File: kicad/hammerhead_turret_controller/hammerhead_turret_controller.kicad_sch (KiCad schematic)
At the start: 7 parts, among them J1 PLATFORM_CONN, J2 B4B-XH-A, J3 B4B-XH-A, J4 B6B-XH-A_LF__SN_, J5 B6B-XH-A_LF__SN_

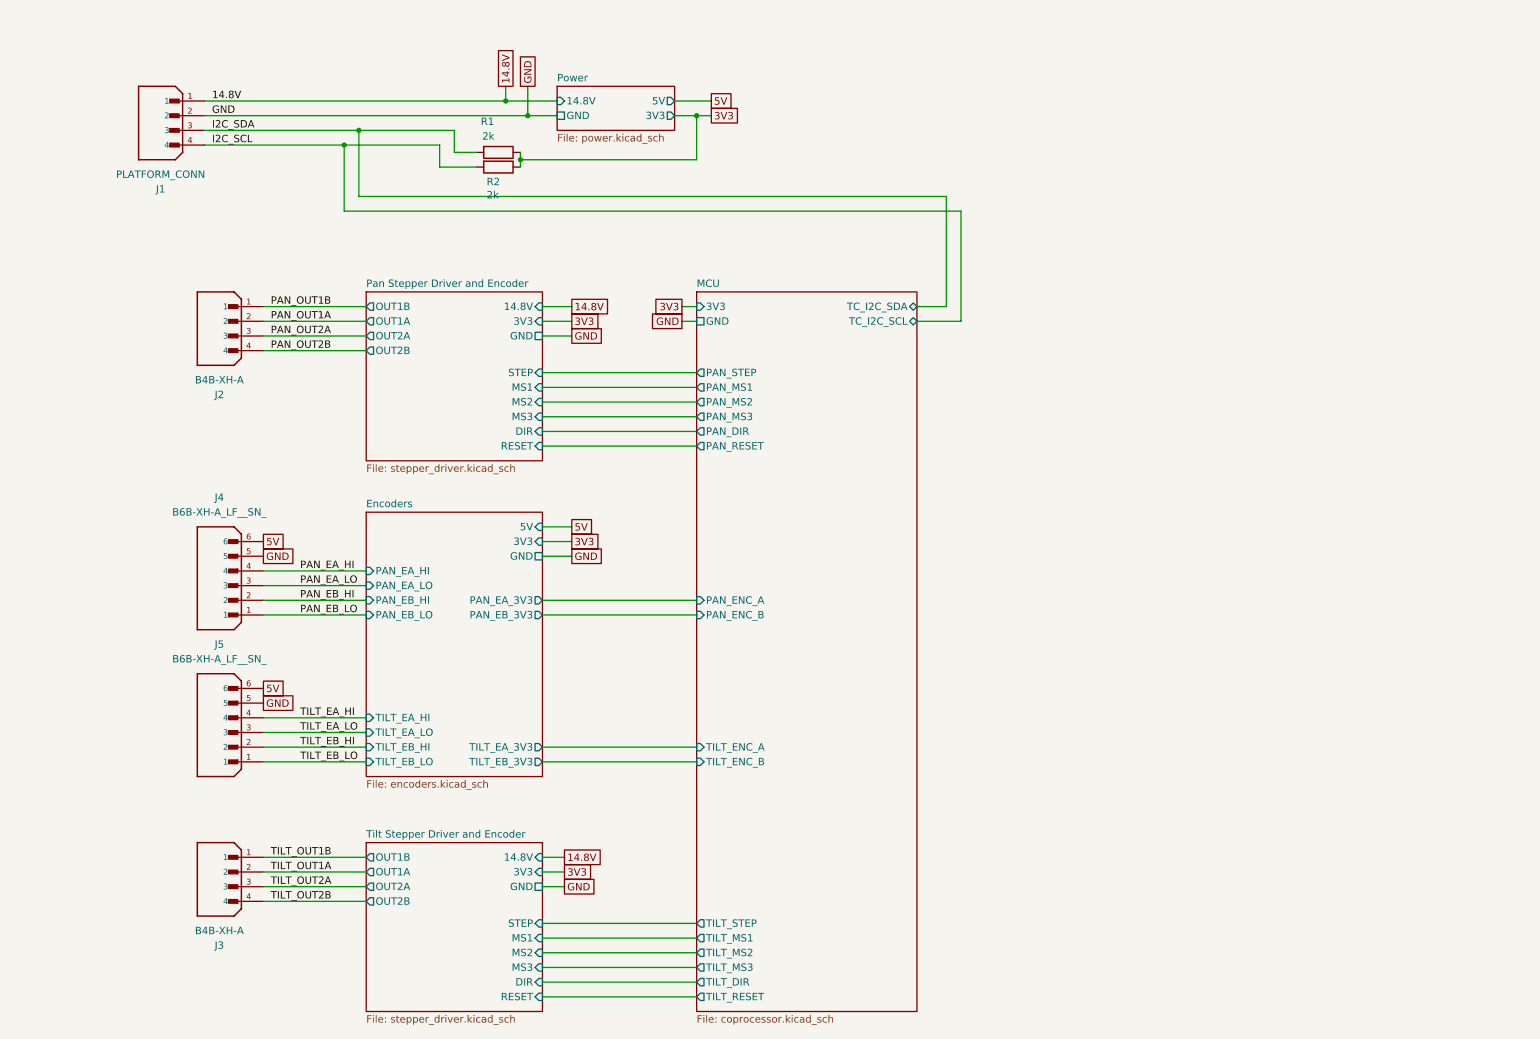
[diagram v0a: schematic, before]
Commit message: add can transceiver
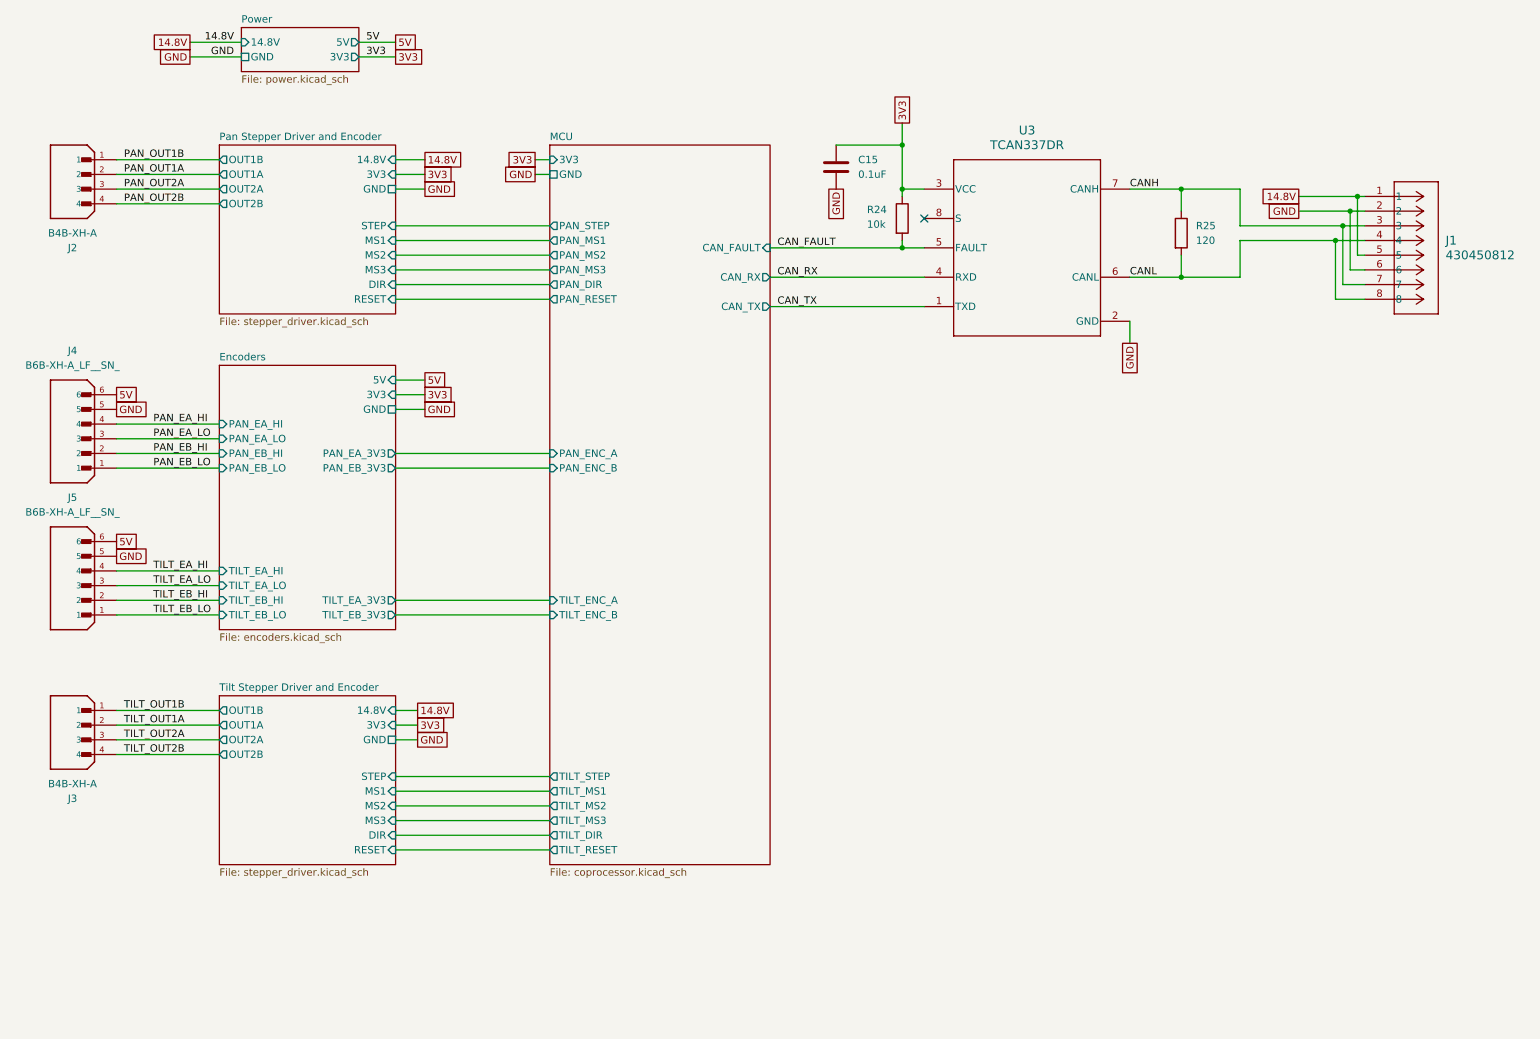
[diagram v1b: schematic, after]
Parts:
- removed J1: PLATFORM_CONN, B4B-XH-A:JST_B4B-XH-A, symbol B4B-XH-A:B4B-XH-A
- removed R1, R2: 2k, Resistor_SMD:R_0201_0603Metric, symbol Device:R
- added C15: 0.1uF, Capacitor_SMD:C_0402_1005Metric, symbol Device:C
- added J1: 430450812, CONN_SD-43045-005_08_MOL, symbol 430450812:430450812
- added R24: 10k, Resistor_SMD:R_0402_1005Metric, symbol Device:R
- added R25: 120, Resistor_SMD:R_0603_1608Metric, symbol Device:R
- added U3: TCAN337DR, TCAN337DR:D0008A_N, symbol TCAN337DR:TCAN337DR
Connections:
- net 14.8V: now also J1.1, J1.5
- net 3V3: now also C15.1, R24.1, U3.3 (VCC)
- net GND: now also C15.2, J1.2, J1.6, U3.2 (GND)
- new net CANH: J1.3, J1.7, R25.1, U3.7 (CANH)
- new net CANL: J1.4, J1.8, R25.2, U3.6 (CANL)
- new net CAN_FAULT: R24.2, U3.5 (FAULT)
- new net CAN_RX: U3.4 (RXD)
- new net CAN_TX: U3.1 (TXD)
- no-connect marks 0 -> 1
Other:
- sheet MCU ports: added CAN_FAULT, CAN_RX, CAN_TX; removed TC_I2C_SCL, TC_I2C_SDA
- moved on the sheet: J2, J3, J4, J5
